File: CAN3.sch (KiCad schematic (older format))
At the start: 33 parts, among them IC17 TJA1055T_3_C,518, IC18 MCP25625T-E_ML, IC19 NCV7356D1R2G, Y2 X322516MLB4SI

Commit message: Checkpoint before trying 4 layer
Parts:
- removed C45: 10nF, Capacitor_SMD:C_0805_2012Metric, symbol Device:CP1
- removed IC17: TJA1055T_3_C,518, SOIC127P600X175-14N, symbol SamacSys_Parts:TJA1055T_3_C,518
- removed JP1, JP10, JP11, JP12, JP13, JP2, JP3, JP4, JP5, JP6, JP7, JP8, JP9: SolderJumper_2_Open, Jumper:SolderJumper-2_P1.3mm_Open_Pad1.0x1.5mm, symbol Jumper:SolderJumper_2_Open
- removed R55: 2K7, Resistor_SMD:R_0805_2012Metric, symbol Device:R_US
- removed R57, R58, R59: 1K, Resistor_SMD:R_0805_2012Metric, symbol Device:R_US
- removed R65: 120R, Resistor_SMD:R_0805_2012Metric, symbol Device:R_US
- IC18: footprint QFN65P600X600X100-29N-D -> Package_SO:SSOP-28_3.9x9.9mm_P0.635mm
- IC19: footprint SOIC127P600X175-8N -> Package_SO:SOIC-14_3.9x8.7mm_P1.27mm
- Y2: footprint X322516MLB4SI -> Crystal:Crystal_SMD_3225-4Pin_3.2x2.5mm
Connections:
- net CAN_EXT3H: now also C47.2, L3.1, R62.1, R63.1
- net RXCAN: now also IC19.4 (RXD), R61.1
- net TXCAN: now also IC19.1 (TXD)
- net RXCAN_HS: no longer names the net of IC18.10 (RXD)
- net TXCAN_HS: no longer names the net of IC18.16 (TXD)
- no-connect marks 11 -> 12

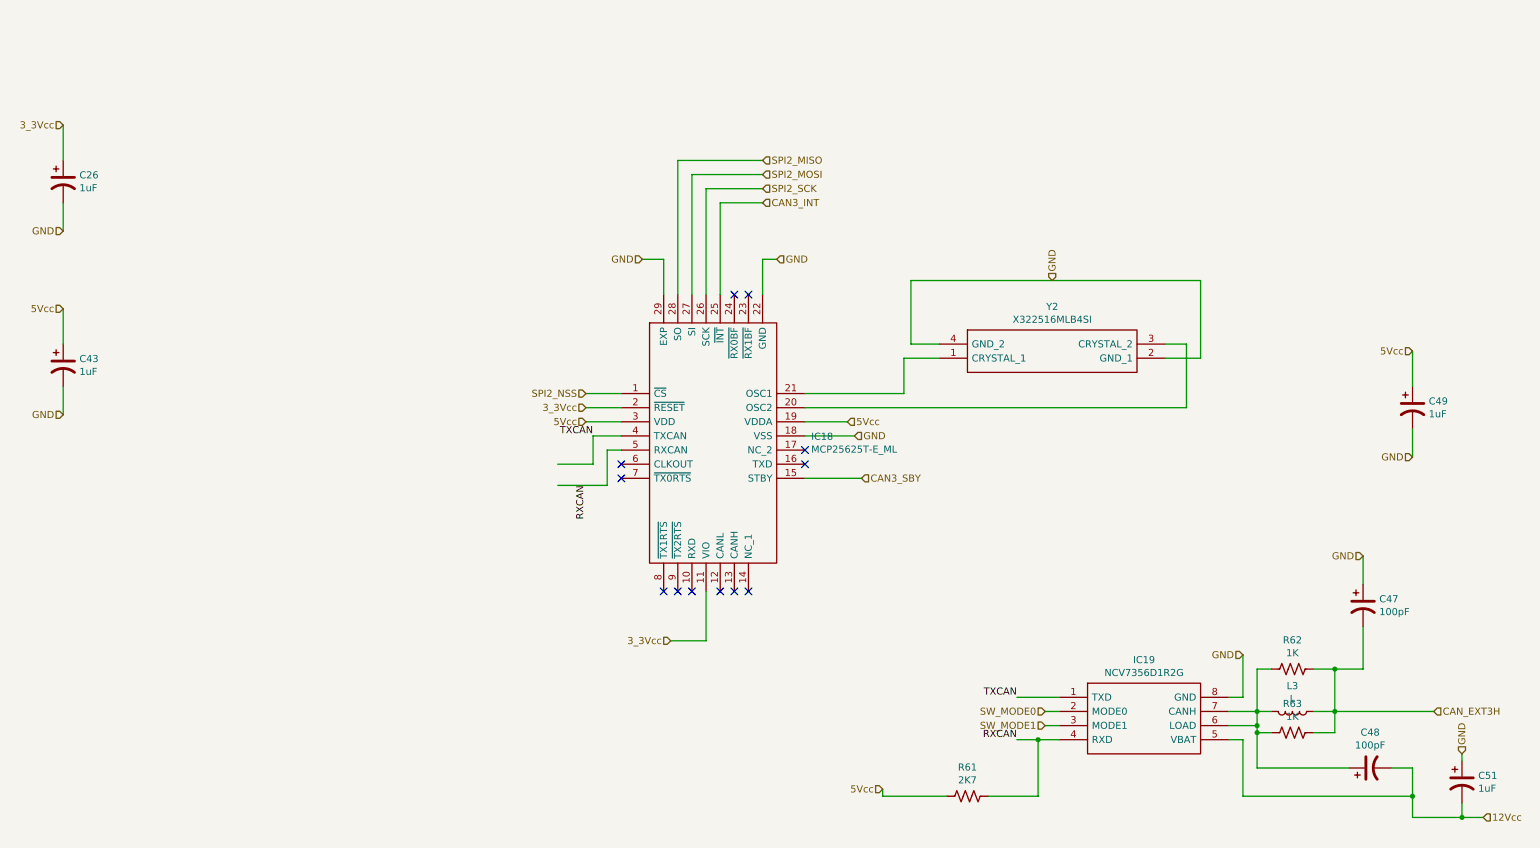
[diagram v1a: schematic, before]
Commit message: Checkpoint 2022-01-19
Design with bluepill to run the heater since we lose some of the SPI
pins to the USB port on the STM32-H107.
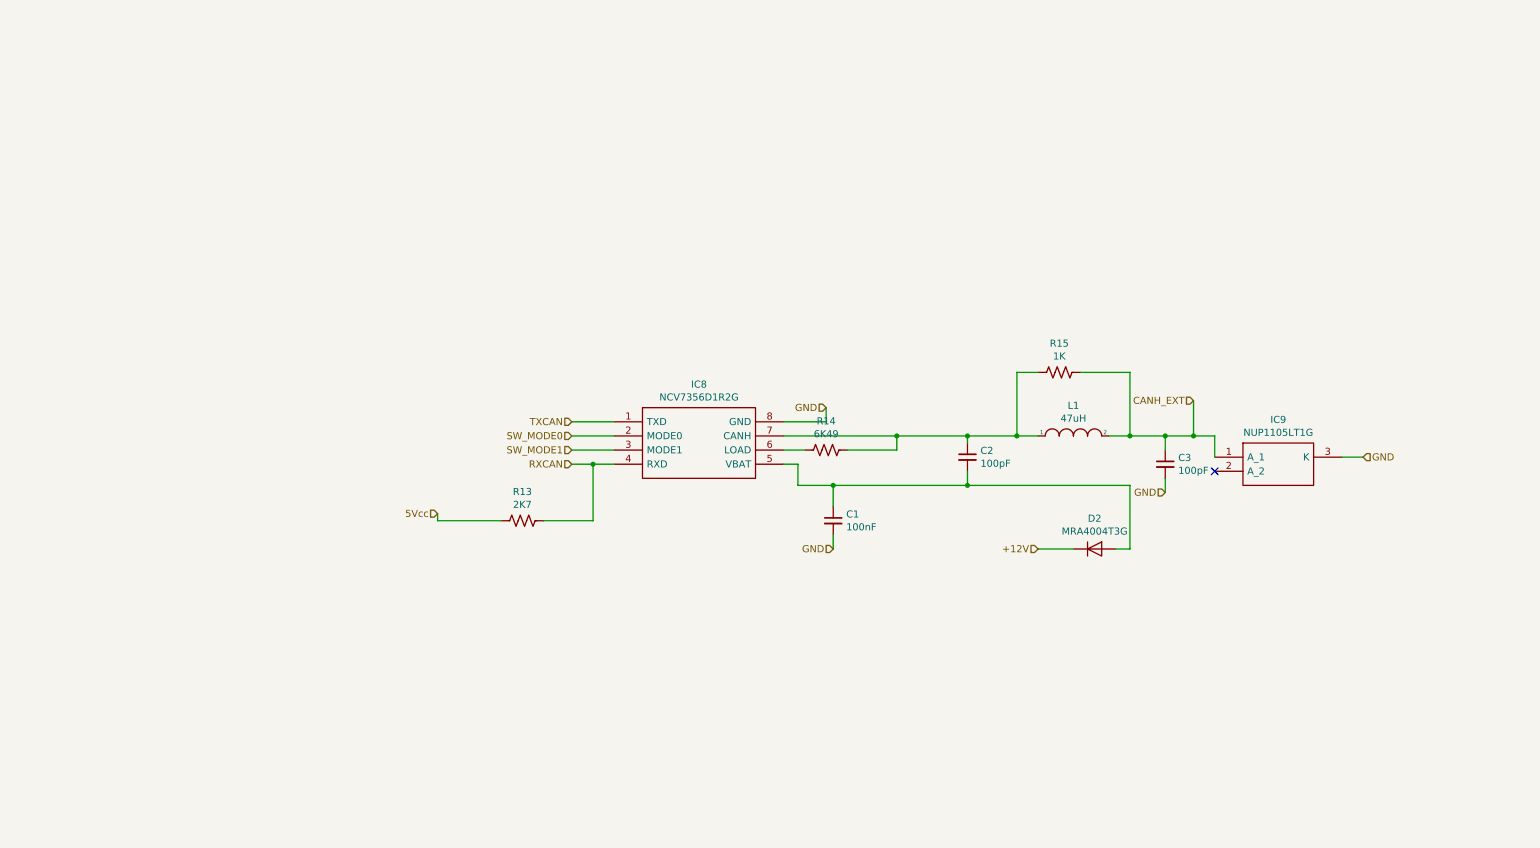
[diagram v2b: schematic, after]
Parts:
- removed C26, C43, C49, C51: 1uF, Capacitor_SMD:C_0805_2012Metric, symbol Device:CP1
- removed C47, C48: 100pF, Capacitor_SMD:C_0805_2012Metric, symbol Device:CP1
- removed IC18: MCP25625T-E_ML, Package_SO:SSOP-28_3.9x9.9mm_P0.635mm, symbol SamacSys_Parts:MCP25625T-E_ML
- removed L3: L, symbol Device:L
- removed R62, R63: 1K, Resistor_SMD:R_0805_2012Metric, symbol Device:R_US
- removed Y2: X322516MLB4SI, Crystal:Crystal_SMD_3225-4Pin_3.2x2.5mm, symbol SamacSys_Parts:X322516MLB4SI
- added C1: 100nF, Capacitor_SMD:C_0805_2012Metric, symbol Device:C_Small
- added C2, C3: 100pF, Capacitor_SMD:C_0805_2012Metric, symbol Device:C_Small
- added D2: MRA4004T3G, Diode_SMD:D_SMA, symbol Diode:MRA4004T3G
- added IC9: NUP1105LT1G, SamacSys_Parts:SOT96P237X111-3N, symbol SamacSys_Parts:NUP1105LT1G
- added L1: 47uH, Inductor_SMD:L_0805_2012Metric, symbol pspice:INDUCTOR
- added R14: 6K49, Resistor_SMD:R_0805_2012Metric, symbol Device:R_US
- added R15: 1K, Resistor_SMD:R_0805_2012Metric, symbol Device:R_US
- renumbered IC19 to IC8, R61 to R13
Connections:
- net GND: now also C1.2, C3.2, IC9.3 (K)
- net at IC8.6 (LOAD): now also R14.2; no longer IC8.7 (CANH)
- net 12Vcc: no longer names the net of IC8.5 (VBAT)
- net 12Vcc: now also C1.1, C2.2, D2.2 (A)
- new net: C2.1, IC8.7 (CANH), L1.1, R14.1, R15.2
- new net +12V: D2.1 (K)
- new net CANH_EXT: C3.1, IC9.1 (A_1), L1.2, R15.1
- no-connect marks 12 -> 1
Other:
- moved on the sheet: IC8, R13
